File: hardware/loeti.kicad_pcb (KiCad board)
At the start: 2 copper layers, 60 x 80 mm, 58 parts, among them J1 USB_C_Receptacle_USB2.0, J2 Samtec FTS-107-01-L-D, J3 AudioJack4, Q1 BC817, Q2 BC817, Q3 BC807, Q4 Si4825DDY, DMG4435SSS, IRF939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, SW1 key2, SW2 SW_SPST, SW3 SW_SPST, U1 AP2204R-3.3, U2 STUSB4500QTR, U3 USBLC6-2SC6, U4 EA_DOGS104B-A, U5 STM32F042K6Tx, U6 ADS1118IDGS, U7 INA138

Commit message: cold junction compensation v3 hardware
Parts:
- removed TP1: WIPE, TestPoint:TestPoint_THTPad_4.0x4.0mm_Drill2.0mm
- added C18: 0.1μF, Capacitor_SMD:C_0603_1608Metric_Pad1.05x0.95mm_HandSolder, F.Cu at (84.4, 68.9)
- added C19: 0.1μF, Capacitor_SMD:C_0603_1608Metric_Pad1.05x0.95mm_HandSolder, F.Cu at (81.0, 42.7)
- added R17: 10k, Resistor_SMD:R_0603_1608Metric_Pad1.05x0.95mm_HandSolder, F.Cu at (87.4, 62.3)
- added R18: 1k, Resistor_SMD:R_0603_1608Metric_Pad1.05x0.95mm_HandSolder, F.Cu at (89.9, 63.2)
- added R19: 1k, Resistor_SMD:R_0603_1608Metric_Pad1.05x0.95mm_HandSolder, F.Cu at (82.8, 68.9)
- added U8: OPA340NA, Package_TO_SOT_SMD:SOT-23-5, F.Cu at (81.0, 45.3)
- R15: value 10m -> CRL2010-FU-R020ELF
- R16: value 1k -> 100k
- moved C16 4.43 mm to (85.2, 43.9), turned to 0 degrees
- moved R3 4.35 mm to (78.6, 68.5), turned to 180 degrees
- moved R2 3.18 mm to (78.6, 66.9), turned to 180 degrees
- moved U6 3.12 mm to (85.2, 48.0), turned to 90 degrees
- moved R13 2.77 mm to (96.4, 60.6), turned to 90 degrees
- moved R16 2.33 mm to (81.0, 48.0), turned to 0 degrees
- moved C12 1.94 mm to (82.2, 79.3), turned to 0 degrees
- moved C10 1.89 mm to (77.6, 79.3), turned to 180 degrees
- moved R6 1.70 mm to (99.4, 68.4)
- moved U7 1.00 mm to (81.0, 50.6)
- moved Q1 0.90 mm to (98.9, 60.7)
- moved R15 0.82 mm to (80.2, 54.2)
- moved D2 0.76 mm to (75.5, 51.6), turned to 45 degrees
- moved C1 0.63 mm to (69.0, 51.2)
- moved U4 0.60 mm to (101.4, 106.7)
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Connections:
- R16 pad 1: ADC_IN2 -> Net-(R16-Pad1)
- U5 pad 13: (no net) -> ADC_IN7
- U7 pad 1: ADC_IN2 -> Net-(R16-Pad1)
- U7 pad 5: SHUNT+ -> +3V3
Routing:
- net ADC_IN2: track 48.3 -> 17.8 mm
- net Net-(R19-Pad1): track 0.00 -> 27.6 mm, vias 0 -> 2
- net ADC_IN7: track 0.00 -> 14.3 mm, vias 0 -> 2
- net +3V3: track 55.2 -> 61.7 mm, vias 20 -> 21
- net SPI1_NSS1: track 26.6 -> 22.9 mm
- net SPI1_SCK: track 45.0 -> 41.3 mm
- net Net-(R16-Pad1): track 0.00 -> 3.59 mm
- net Net-(SW3-Pad1): track 54.9 -> 51.5 mm
- net LCD_NRST: track 16.5 -> 13.5 mm
- net I2C1_SDA: track 10.9 -> 13.8 mm
- net PA5: track 22.2 -> 19.4 mm
- net Net-(Q1-Pad3): track 9.18 -> 6.54 mm
- net SHUNT+: track 42.7 -> 40.1 mm
- net Net-(SW2-Pad1): track 50.9 -> 48.3 mm
- net PD_RST: track 29.8 -> 32.1 mm, vias 2 -> 3
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- added copper zone on F.Cu, net SHUNT-
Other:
- outline, holes or cut-outs redrawn
- board text added: "X"
- board text added: "af 2020"
- board text added: "fairy edition"
- board text added: "v3"
- board text removed: "af 2020 v2"
- board text removed: "sophi edition"

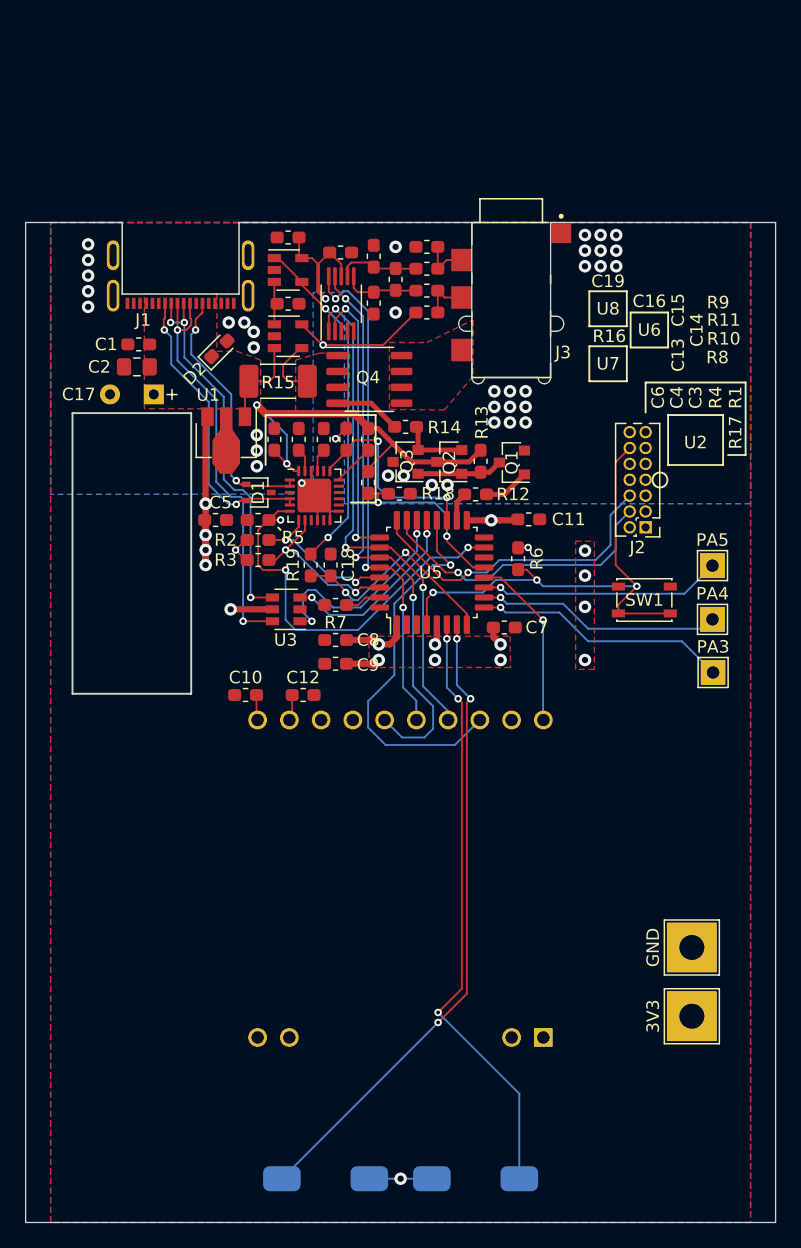
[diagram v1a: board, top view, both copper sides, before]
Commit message: Switched to chibios 20.3.1
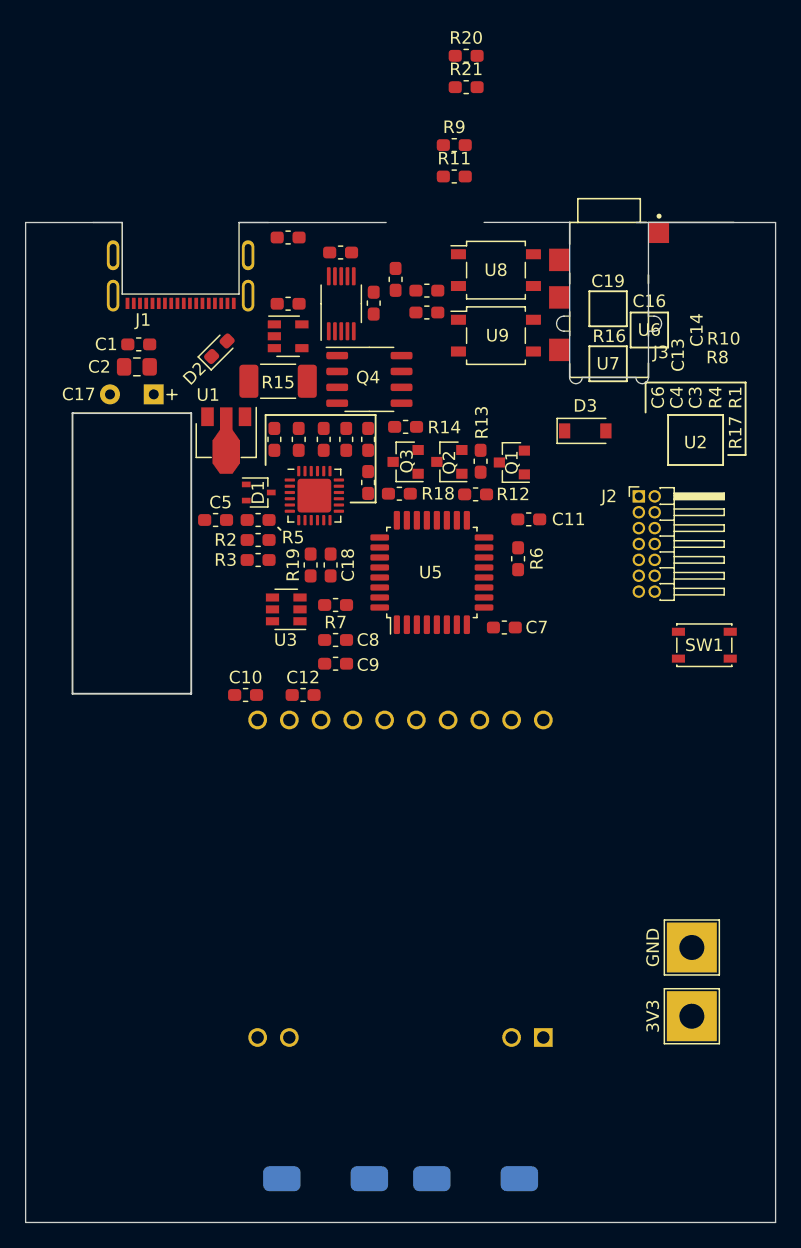
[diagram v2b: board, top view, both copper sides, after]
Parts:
- removed C15: 0.1μF, Capacitor_SMD:C_0603_1608Metric_Pad1.05x0.95mm_HandSolder
- removed TP4: PA3, TestPoint:TestPoint_THTPad_2.0x2.0mm_Drill1.0mm
- removed TP5: PA4, TestPoint:TestPoint_THTPad_2.0x2.0mm_Drill1.0mm
- removed TP6: PA5, TestPoint:TestPoint_THTPad_2.0x2.0mm_Drill1.0mm
- added D3: D_Schottky, Diode_SMD:D_SOD-123, F.Cu at (104.8, 58.2)
- added R20: 470, Resistor_SMD:R_0603_1608Metric_Pad1.05x0.95mm_HandSolder, F.Cu at (95.2, 28.2)
- added R21: 470, Resistor_SMD:R_0603_1608Metric_Pad1.05x0.95mm_HandSolder, F.Cu at (95.2, 30.7)
- added U9: ASSR-1218, Package_SO:SO-4_4.4x4.3mm_P2.54mm, F.Cu at (97.6, 50.5)
- J2: value Samtec FTS-107-01-L-D -> 20021112-00014T1LF; footprint Connector_PinHeader_1.27mm:PinHeader_2x07_P1.27mm_Vertical -> Connector_PinHeader_1.27mm:PinHeader_2x07_P1.27mm_Horizontal
- R10: value 470 -> 47
- R11: value 470 -> 20
- R15: value CRL2010-FU-R020ELF -> WSL2010R0200FEA18
- R19: value 1k -> 10k
- R9: value 1M -> 20
- U8: value OPA340NA -> ASSR-1218; footprint Package_TO_SOT_SMD:SOT-23-5 -> Package_SO:SO-4_4.4x4.3mm_P2.54mm
- moved U8 16.6 mm to (97.6, 45.3)
- moved R9 8.43 mm to (94.3, 35.3), turned to 0 degrees
- moved J3 7.83 mm to (106.7, 47.7)
- moved R11 7.70 mm to (94.3, 37.8), turned to 0 degrees
- moved SW1 6.01 mm to (114.3, 75.3)
- moved J2 2.54 mm to (109.1, 63.4), turned to 0 degrees
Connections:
- C14 pad 1: Net-(C14-Pad1) -> HEATER-
- J3 pad R2: T- -> HEATER-
- R10 pad 1: T+ -> Net-(R10-Pad1)
- R11 pad 1: T- -> Net-(R11-Pad1)
- R11 pad 2: Net-(C14-Pad1) -> USB_P
- R19 pad 1: Net-(R19-Pad1) -> (no net)
- R8 pad 1: T+ -> Net-(R10-Pad1)
- R9 pad 1: T- -> Net-(R9-Pad1)
- R9 pad 2: HEATER- -> USB_N
- U5 pad 10: PA4 -> SEL_TC_0
- U5 pad 11: PA5 -> (no net)
- U5 pad 21: USB_N -> Net-(R9-Pad1)
- U5 pad 22: USB_P -> Net-(R11-Pad1)
- U5 pad 9: PA3 -> SEL_TC_1
- U6 pad 7: Net-(C14-Pad1) -> HEATER-
- U8 pad 1: Net-(R19-Pad1) -> Net-(R20-Pad1)
- U8 pad 3: Net-(R16-Pad1) -> T+
- U8 pad 4: Net-(R19-Pad1) -> Net-(R10-Pad1)
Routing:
- net +3V3: track 61.7 -> 0.00 mm, vias 21 -> 0
- net Net-(SW3-Pad1): track 51.5 -> 0.00 mm, vias 3 -> 0
- net Net-(SW2-Pad1): track 48.3 -> 0.00 mm, vias 3 -> 0
- net SPI1_MISO: track 46.3 -> 0.00 mm, vias 3 -> 0
- net SPI1_SCK: track 41.3 -> 0.00 mm, vias 3 -> 0
- net SPI1_MOSI: track 41.2 -> 0.00 mm, vias 3 -> 0
- net NRST: track 40.7 -> 0.00 mm, vias 3 -> 0
- net SHUNT+: track 40.1 -> 0.00 mm, vias 2 -> 0
- net Net-(J1-PadA6): track 33.4 -> 0.00 mm, vias 2 -> 0
- net PD_RST: track 32.1 -> 0.00 mm, vias 3 -> 0
- net SPI1_NSS2: track 30.9 -> 0.00 mm, vias 1 -> 0
- net Net-(J1-PadA7): track 30.6 -> 0.00 mm, vias 3 -> 0
- net Net-(R19-Pad1): track 27.6 -> 0.00 mm, vias 2 -> 0
- net SWCLK: track 25.5 -> 0.00 mm, vias 1 -> 0
- net CC2: track 24.1 -> 0.00 mm, vias 2 -> 0
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- removed copper zone on B.Cu, net +3V3
- removed copper zone on F.Cu, net +3V3
- removed copper zone on F.Cu, net HEATER+
- removed copper zone on B.Cu, net HEATER-
- removed copper zone on F.Cu, net HEATER-
- removed copper zone on F.Cu, net SHUNT+
- removed copper zone on F.Cu, net SHUNT-
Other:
- copper layers 2 -> 4

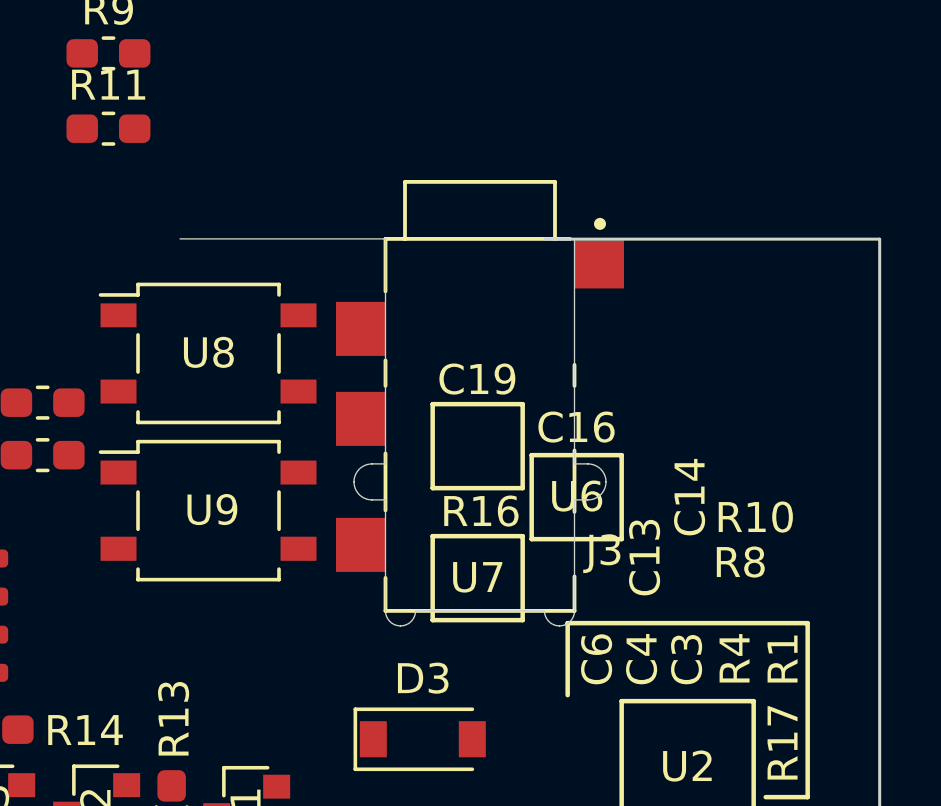
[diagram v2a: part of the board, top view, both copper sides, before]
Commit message: Ported to ChibiOS 20
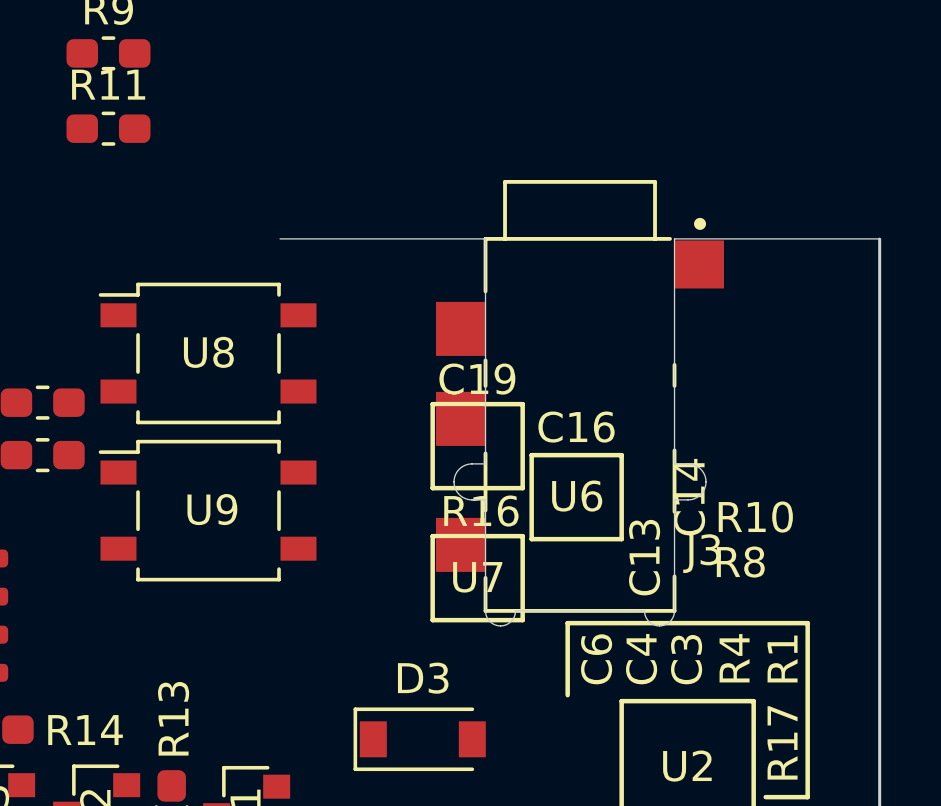
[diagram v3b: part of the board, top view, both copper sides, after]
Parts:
- moved J3 3.33 mm to (110.0, 47.7)
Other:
- outline, holes or cut-outs redrawn
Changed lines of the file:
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@@
   (general
     (thickness 1.6)
-    (drawings 41)
+    (drawings 40)
     (tracks 0)
     (zones 0)
@@
   )
   (module custom:CUI_SJ-43614-SMT (layer F.Cu)
-    (at 106.6774 47.6919 270)
+    (at 110.0115 47.6919 270)
     (fp_text reference J3 (at 4.2 -4.15 180) (layer F.SilkS)
       (effects (font (size 1.000228 1.000228) (thickness 0.15)))
@@
   (gr_line (start 120 121.5) (end 60 121.5) (layer Edge.Cuts) (width 0.1))
   (gr_line (start 120 41.5) (end 120 121.5) (layer Edge.Cuts) (width 0.1))
-  (gr_line (start 108.85 41.5) (end 120 41.5) (layer Edge.Cuts) (width 0.1))
   (gr_line (start 60 41.5) (end 65.4 41.5) (layer Edge.Cuts) (width 0.1))
   (gr_line (start 60 41.5) (end 60 121.5) (layer Edge.Cuts) (width 0.1))

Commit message: v4, stusb final
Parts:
- added D4: BAT54S, Package_TO_SOT_SMD:SOT-23, F.Cu at (82.0, 73.5)
- added D5: BAT54S, Package_TO_SOT_SMD:SOT-23, F.Cu at (89.4, 77.7)
- added R22: 10k, Resistor_SMD:R_0603_1608Metric_Pad1.05x0.95mm_HandSolder, F.Cu at (81.8, 69.1)
- J3: value AudioJack4 -> AudioJack3; footprint custom:CUI_SJ-43614-SMT -> custom:CUI_SJ-3502-SMT
- R16: value 100k -> DNP
- U7: value INA138 -> INA301; footprint Package_TO_SOT_SMD:SOT-23-5 -> Package_SO:VSSOP-8_3.0x3.0mm_P0.65mm
- moved C5 46.6 mm to (116.8, 44.3), turned to 270 degrees
- moved C2 45.3 mm to (114.1, 51.4), turned to 0 degrees
- moved C1 45.2 mm to (114.2, 49.5), turned to 0 degrees
- moved C17 42.1 mm to (112.3, 53.6), turned to 0 degrees
- moved SW1 40.7 mm to (73.6, 75.7)
- moved U1 39.7 mm to (113.4, 45.1), turned to 180 degrees
- moved R20 37.5 mm to (73.4, 58.7), turned to 270 degrees
- moved J2 37.4 mm to (72.6, 71.7), turned to 180 degrees
- moved R9 35.4 mm to (96.0, 70.7)
- moved J3 33.6 mm to (76.4, 47.9)
- moved R21 32.2 mm to (79.4, 58.7), turned to 270 degrees
- moved R11 31.3 mm to (96.0, 69.1)
- moved J1 30.6 mm to (103.0, 41.5)
- moved R6 30.5 mm to (69.8, 75.7)
- moved U8 29.8 mm to (70.0, 56.5), turned to 90 degrees
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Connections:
- R16 pad 1: Net-(R16-Pad1) -> HEATER-
- R16 pad 2: HEATER- -> CUR_LIMIT
- R19 pad 1: (no net) -> Net-(R19-Pad1)
- U5 pad 2: (no net) -> CUR_RESET
- U5 pad 3: (no net) -> CUR_NALERT
- U7 pad 1: Net-(R16-Pad1) -> +3V3
- U7 pad 2: HEATER- -> Net-(R19-Pad1)
- U7 pad 3: SHUNT+ -> CUR_LIMIT
- U7 pad 4: SHUNT- -> HEATER-
- U7 pad 5: +3V3 -> CUR_RESET
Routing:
- net SPI1_SCK: track 0.00 -> 64.5 mm, vias 0 -> 2
- net SPI1_MISO: track 0.00 -> 59.2 mm, vias 0 -> 2
- net HEATER-: track 0.00 -> 57.0 mm, vias 0 -> 31
- net SPI1_MOSI: track 0.00 -> 55.3 mm, vias 0 -> 2
- net Net-(SW2-Pad1): track 0.00 -> 53.7 mm, vias 0 -> 2
- net Net-(SW3-Pad1): track 0.00 -> 49.6 mm, vias 0 -> 2
- net SHUNT+: track 0.00 -> 44.7 mm
- net SPI1_NSS1: track 0.00 -> 44.7 mm, vias 0 -> 2
- net ADC_IN2: track 0.00 -> 39.6 mm, vias 0 -> 2
- net NRST: track 0.00 -> 35.4 mm, vias 0 -> 2
- net CUR_LIMIT: track 0.00 -> 31.9 mm, vias 0 -> 2
- net SEL_TC_0: track 0.00 -> 29.0 mm
- net SWDIO: track 0.00 -> 28.8 mm, vias 0 -> 2
- net SWCLK: track 0.00 -> 28.4 mm, vias 0 -> 1
- net CUR_NALERT: track 0.00 -> 28.1 mm, vias 0 -> 2
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- added copper zone on In1.Cu, net +3V3
- added copper zone on F.Cu, net HEATER+
- added copper zone on B.Cu, net HEATER-
- added copper zone on F.Cu, net HEATER-
- added copper zone on In2.Cu, net HEATER-
- added copper zone on F.Cu, net SHUNT+
- added copper zone on F.Cu, net SHUNT-
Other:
- outline, holes or cut-outs redrawn
- board text added: "hawki edition"
- board text added: "v4"
- board text removed: "X"
- board text removed: "fairy edition"
- board text removed: "v3"

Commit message: v4 production version
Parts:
- removed R11, R9: 20, Resistor_SMD:R_0603_1608Metric_Pad1.05x0.95mm_HandSolder
- removed R21: 470, Resistor_SMD:R_0603_1608Metric_Pad1.05x0.95mm_HandSolder
- removed U3: USBLC6-2SC6, Package_TO_SOT_SMD:SOT-23-6
- R15: value WSL2010R0200FEA18 -> WSLP2010R0100FEA
- R16: value DNP -> 25k
- U5: value STM32F042K6Tx -> STM32F030K6Tx
- U7: value INA301 -> INA301A
- moved C7 1.84 mm to (97.4, 67.7)
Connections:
- net Net-(R7-Pad2) renamed BOOT0
- J1 pad A6: Net-(J1-PadA6) -> (no net)
- J1 pad A7: Net-(J1-PadA7) -> (no net)
- J1 pad B6: Net-(J1-PadA6) -> (no net)
- J1 pad B7: Net-(J1-PadA7) -> (no net)
- J2 pad 13: (no net) -> VCP_RX
- J2 pad 14: (no net) -> VCP_TX
- U5 pad 19: PD_ALERT_INT -> VCP_RX
- U5 pad 20: SPI1_NSS2 -> VCP_TX
- U5 pad 21: Net-(R9-Pad1) -> PD_ALERT_INT
- U5 pad 22: Net-(R11-Pad1) -> SPI1_NSS2
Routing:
- net CUR_LIMIT: track 31.9 -> 2.32 mm, vias 2 -> 0
- net Net-(J1-PadA7): track 27.3 -> 0.00 mm, vias 2 -> 0
- net VCP_TX: track 0.00 -> 26.2 mm, vias 0 -> 1
- net VCP_RX: track 0.00 -> 24.9 mm, vias 0 -> 1
- net Net-(J1-PadA6): track 24.7 -> 0.00 mm, vias 3 -> 0
- net PD_RST: track 24.9 -> 21.8 mm
- net CC2: track 13.0 -> 15.5 mm
- net Net-(R9-Pad1): track 2.09 -> 0.00 mm
- net Net-(R11-Pad1): track 2.09 -> 0.00 mm
- net USB_P: track 1.89 -> 0.00 mm
- net USB_N: track 1.89 -> 0.00 mm
- net CC1: track 13.6 -> 15.4 mm
- net ADC_IN2: track 39.6 -> 40.6 mm
- net HEATER-: track 57.0 -> 56.2 mm, vias 31 -> 30
- net PD_ALERT_INT: track 19.7 -> 19.1 mm
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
